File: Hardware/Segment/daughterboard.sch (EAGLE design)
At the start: 170 parts, among them IC1 PBQ79656PAPTQ1, IC2 PBQ79656PAPTQ1, T1 PBHV8115X, 115, T2 PBHV8115X, 115

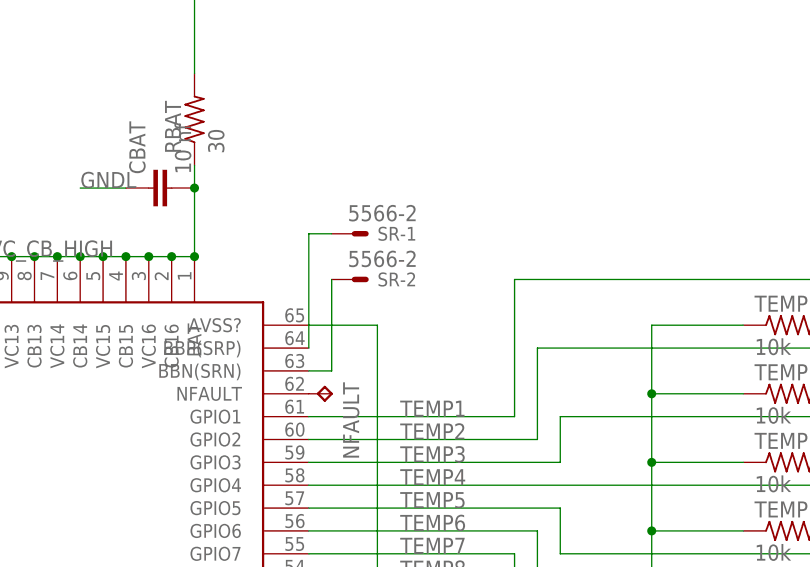
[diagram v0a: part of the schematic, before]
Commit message: Work on BQ library, RC fix for SR
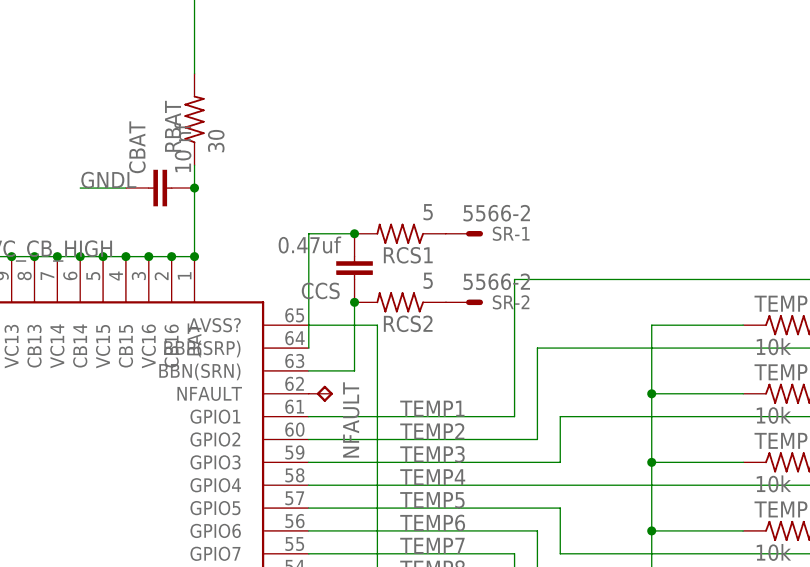
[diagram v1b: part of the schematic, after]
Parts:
- added CCS: 0.47uf, rcl:C-EUC0603
- added RCS1, RCS2: 5, rcl:R-US_R0603
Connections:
- new net N$13: RCS2.1, SR-2.S
- new net N$16: RCS1.1, SR-1.S
- net N$4: now also CCS.2, RCS1.2; no longer SR-1.S
- net N$7: now also CCS.1, RCS2.2; no longer SR-2.S
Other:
- moved on the sheet: SR-1, SR-2
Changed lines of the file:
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@@
 <part name="GND" library="wirepad" library_urn="urn:adsk.eagle:library:412" deviceset="2,54/1,0" device="" package3d_urn="urn:adsk.eagle:package:30828/1"/>
 <part name="NFAULT" library="testpad" library_urn="urn:adsk.eagle:library:385" deviceset="TP" device="B2,54" package3d_urn="urn:adsk.eagle:package:27948/1"/>
+<part name="RCS1" library="rcl" library_urn="urn:adsk.eagle:library:334" deviceset="R-US_" device="R0603" package3d_urn="urn:adsk.eagle:package:23555/3" value="5"/>
+<part name="RCS2" library="rcl" library_urn="urn:adsk.eagle:library:334" deviceset="R-US_" device="R0603" package3d_urn="urn:adsk.eagle:package:23555/3" value="5"/>
+<part name="CCS" library="rcl" library_urn="urn:adsk.eagle:library:334" deviceset="C-EU" device="C0603" package3d_urn="urn:adsk.eagle:package:23616/2" value="0.47uf"/>
 </parts>
 <sheets>
@@
 <attribute name="VALUE" x="181.737" y="198.882" size="1.778" layer="96" rot="R270"/>
 </instance>
-<instance part="SR" gate="-1" x="195.58" y="86.36" smashed="yes">
-<attribute name="NAME" x="198.12" y="85.598" size="1.524" layer="95"/>
-<attribute name="VALUE" x="194.818" y="87.757" size="1.778" layer="96"/>
-</instance>
-<instance part="SR" gate="-2" x="195.58" y="81.28" smashed="yes">
-<attribute name="NAME" x="198.12" y="80.518" size="1.524" layer="95"/>
-<attribute name="VALUE" x="194.818" y="82.677" size="1.778" layer="96"/>
+<instance part="SR" gate="-1" x="208.28" y="86.36" smashed="yes">
+<attribute name="NAME" x="210.82" y="85.598" size="1.524" layer="95"/>
+<attribute name="VALUE" x="207.518" y="87.757" size="1.778" layer="96"/>
+</instance>
+<instance part="SR" gate="-2" x="208.28" y="78.74" smashed="yes">
+<attribute name="NAME" x="210.82" y="77.978" size="1.524" layer="95"/>
+<attribute name="VALUE" x="207.518" y="80.137" size="1.778" layer="96"/>
 </instance>
 <instance part="DISABLE_UART" gate="1" x="175.26" y="43.18" smashed="yes">
@@
 <attribute name="TP_SIGNAL_NAME" x="191.77" y="67.31" size="1.778" layer="97" rot="R270"/>
 </instance>
+<instance part="RCS1" gate="G$1" x="200.66" y="86.36" smashed="yes" rot="R180">
+<attribute name="NAME" x="204.47" y="84.8614" size="1.778" layer="95" rot="R180"/>
+<attribute name="VALUE" x="204.47" y="89.662" size="1.778" layer="96" rot="R180"/>
+</instance>
+<instance part="RCS2" gate="G$1" x="200.66" y="78.74" smashed="yes" rot="R180">
+<attribute name="NAME" x="204.47" y="77.2414" size="1.778" layer="95" rot="R180"/>
+<attribute name="VALUE" x="204.47" y="82.042" size="1.778" layer="96" rot="R180"/>
+</instance>
+<instance part="CCS" gate="G$1" x="195.58" y="81.28" smashed="yes" rot="R180">
+<attribute name="NAME" x="194.056" y="80.899" size="1.778" layer="95" rot="R180"/>
+<attribute name="VALUE" x="194.056" y="85.979" size="1.778" layer="96" rot="R180"/>
+</instance>
 </instances>
 <busses>
@@
 <pinref part="IC1" gate="G$1" pin="BBP(SRP)"/>
 <wire x1="190.5" y1="73.66" x2="190.5" y2="86.36" width="0.1524" layer="91"/>
-<pinref part="SR" gate="-1" pin="S"/>
-<wire x1="190.5" y1="86.36" x2="193.04" y2="86.36" width="0.1524" layer="91"/>
+<pinref part="CCS" gate="G$1" pin="2"/>
+<pinref part="RCS1" gate="G$1" pin="2"/>
+<wire x1="190.5" y1="86.36" x2="195.58" y2="86.36" width="0.1524" layer="91"/>
+<junction x="195.58" y="86.36"/>
 </segment>
 </net>
 <net name="N$7" class="0">
 <segment>
-<pinref part="SR" gate="-2" pin="S"/>
-<wire x1="193.04" y1="81.28" x2="193.04" y2="71.12" width="0.1524" layer="91"/>
 <pinref part="IC1" gate="G$1" pin="BBN(SRN)"/>
-<wire x1="193.04" y1="71.12" x2="190.5" y2="71.12" width="0.1524" layer="91"/>
+<pinref part="CCS" gate="G$1" pin="1"/>
+<pinref part="RCS2" gate="G$1" pin="2"/>
+<wire x1="190.5" y1="71.12" x2="195.58" y2="71.12" width="0.1524" layer="91"/>
+<wire x1="195.58" y1="71.12" x2="195.58" y2="78.74" width="0.1524" layer="91"/>
+<junction x="195.58" y="78.74"/>
 </segment>
 </net>
@@
 </segment>
 </net>
+<net name="N$13" class="0">
+<segment>
+<pinref part="RCS2" gate="G$1" pin="1"/>
+<pinref part="SR" gate="-2" pin="S"/>
+</segment>
+</net>
+<net name="N$16" class="0">
+<segment>
+<pinref part="SR" gate="-1" pin="S"/>
+<pinref part="RCS1" gate="G$1" pin="1"/>
+</segment>
+</net>

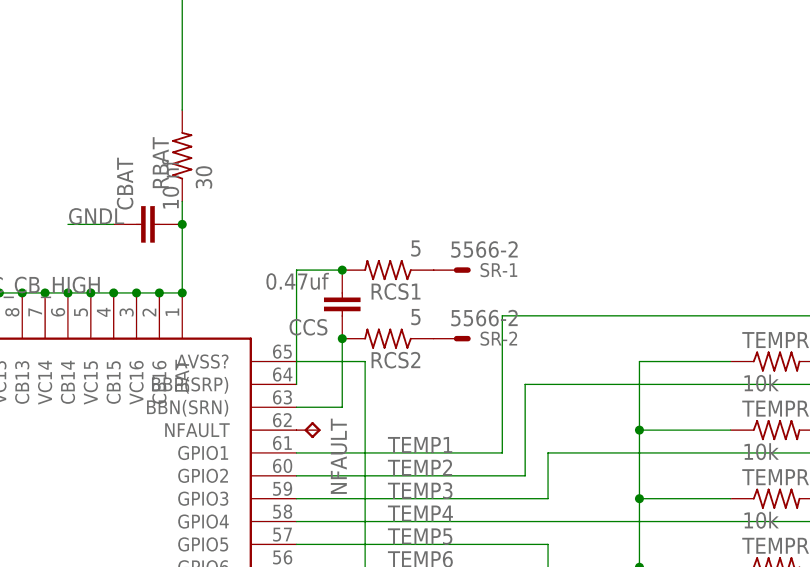
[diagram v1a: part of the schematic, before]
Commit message: ESP32-devkitc-32D instead ov DEVKIT V1
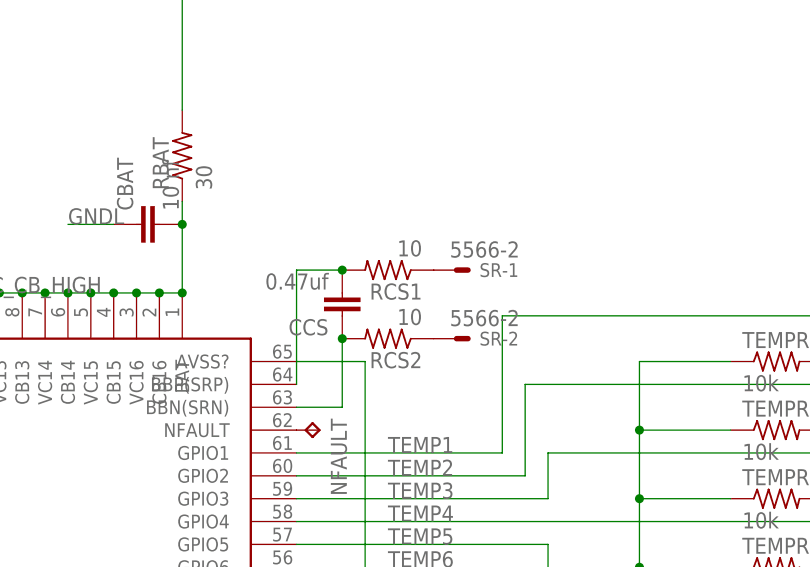
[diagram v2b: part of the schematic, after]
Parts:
- RCS1, RCS2: value 5 -> 10
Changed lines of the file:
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@@
 <part name="GND" library="wirepad" library_urn="urn:adsk.eagle:library:412" deviceset="2,54/1,0" device="" package3d_urn="urn:adsk.eagle:package:30828/1"/>
 <part name="NFAULT" library="testpad" library_urn="urn:adsk.eagle:library:385" deviceset="TP" device="B2,54" package3d_urn="urn:adsk.eagle:package:27948/1"/>
-<part name="RCS1" library="rcl" library_urn="urn:adsk.eagle:library:334" deviceset="R-US_" device="R0603" package3d_urn="urn:adsk.eagle:package:23555/3" value="5"/>
-<part name="RCS2" library="rcl" library_urn="urn:adsk.eagle:library:334" deviceset="R-US_" device="R0603" package3d_urn="urn:adsk.eagle:package:23555/3" value="5"/>
+<part name="RCS1" library="rcl" library_urn="urn:adsk.eagle:library:334" deviceset="R-US_" device="R0603" package3d_urn="urn:adsk.eagle:package:23555/3" value="10"/>
+<part name="RCS2" library="rcl" library_urn="urn:adsk.eagle:library:334" deviceset="R-US_" device="R0603" package3d_urn="urn:adsk.eagle:package:23555/3" value="10"/>
 <part name="CCS" library="rcl" library_urn="urn:adsk.eagle:library:334" deviceset="C-EU" device="C0603" package3d_urn="urn:adsk.eagle:package:23616/2" value="0.47uf"/>
 </parts>

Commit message: Fixed resistors in layout, moved connectors from edge
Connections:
- removed net N$100: CVC0-1.1, CVC1-1.2, RVC1-1.1, VCH-2.S
- removed net N$101: CVC1-1.1, CVC2-1.2, RVC2-1.1, VCH-3.S
- removed net N$102: CVC2-1.1, CVC3-1.2, RVC3-1.1, VCH-4.S
- removed net N$103: CVC3-1.1, CVC4-1.2, RVC4-1.1, VCH-5.S
- removed net N$104: CVC4-1.1, CVC5-1.2, RVC5-1.1, VCH-6.S
- removed net N$105: CVC5-1.1, CVC6-1.2, RVC6-1.1, VCH-7.S
- removed net N$106: CVC6-1.1, CVC7-1.2, RVC7-1.1, VCH-8.S
- removed net N$107: CVC7-1.1, CVC8-1.2, RVC8-1.1, VCH-9.S
- removed net N$108: CVC8-1.1, CVC9-1.2, RVC9-1.1, VCH-10.S
- removed net N$109: CVC9-1.1, RVC10-1.1, VCH-11.S
- removed net N$43: CVC8.1, CVC9.2, RVC9.1, VCL-10.S
- removed net N$44: CVC9.1, RVC10.1, VCL-11.S
- removed net N$99: CVC0-1.2, RVC0-1.1, VCH-1.S
- new net N$11: CBL-11.S, RCB10.1
- new net N$17: CBH-11.S, RCB10-1.1
- new net N$19: RVC1.1, VCL-2.S
- new net N$20: RVC2.1, VCL-3.S
- new net N$22: RVC3.1, VCL-4.S
- new net N$23: RVC4.1, VCL-5.S
- new net N$24: RVC9.1, VCL-10.S
- new net N$25: RVC8.1, VCL-9.S
- new net N$26: RVC7.1, VCL-8.S
- new net N$28: RVC6.1, VCL-7.S
- new net N$30: RVC5.1, VCL-6.S
- new net N$32: CBL-1.S, RCB0.1
- new net N$96: CBH-1.S, RCB0-1.1
- net BATC: now also RVC10.1, VCL-11.S; no longer CBL-11.S, RCB10.1
- net BATC-1: now also RVC10-1.1, VCH-11.S; no longer CBH-11.S, RCB10-1.1
- net GNDH: now also RVC0-1.1, VCH-1.S; no longer CBH-1.S, RCB0-1.1
- net GNDL: now also RVC0.1, VCL-1.S; no longer CBL-1.S, RCB0.1
- net N$34: now also RVC9-1.1, VCH-10.S; no longer CVC0.2, RVC0.1, VCL-1.S
- net N$35: now also RVC8-1.1, VCH-9.S; no longer CVC0.1, CVC1.2, RVC1.1, VCL-2.S
- net N$36: now also RVC7-1.1, VCH-8.S; no longer CVC1.1, CVC2.2, RVC2.1, VCL-3.S
- net N$37: now also RVC6-1.1, VCH-7.S; no longer CVC2.1, CVC3.2, RVC3.1, VCL-4.S
- net N$38: now also RVC5-1.1, VCH-6.S; no longer CVC3.1, CVC4.2, RVC4.1, VCL-5.S
- net N$39: now also RVC4-1.1, VCH-5.S; no longer CVC4.1, CVC5.2, RVC5.1, VCL-6.S
- net N$40: now also RVC3-1.1, VCH-4.S; no longer CVC5.1, CVC6.2, RVC6.1, VCL-7.S
- net N$41: now also RVC2-1.1, VCH-3.S; no longer CVC6.1, CVC7.2, RVC7.1, VCL-8.S
- net N$42: now also RVC1-1.1, VCH-2.S; no longer CVC7.1, CVC8.2, RVC8.1, VCL-9.S
- net VC0: now also CVC0.2
- net VC0-1: now also CVC0-1.2
- net VC1: now also CVC0.1, CVC1.2
- net VC1-1: now also CVC0-1.1, CVC1-1.2
- net VC10: now also CVC9.1
- net VC10-1: now also CVC9-1.1
- net VC2: now also CVC1.1, CVC2.2
- net VC2-1: now also CVC1-1.1, CVC2-1.2
- net VC3: now also CVC2.1, CVC3.2
- net VC3-1: now also CVC2-1.1, CVC3-1.2
- net VC4: now also CVC3.1, CVC4.2
- net VC4-1: now also CVC3-1.1, CVC4-1.2
- net VC5: now also CVC4.1, CVC5.2
- net VC5-1: now also CVC4-1.1, CVC5-1.2
- net VC6: now also CVC5.1, CVC6.2
- net VC6-1: now also CVC5-1.1, CVC6-1.2
- net VC7: now also CVC6.1, CVC7.2
- net VC7-1: now also CVC6-1.1, CVC7-1.2
- net VC8: now also CVC7.1, CVC8.2
- net VC8-1: now also CVC7-1.1, CVC8-1.2
- net VC9: now also CVC8.1, CVC9.2
- net VC9-1: now also CVC8-1.1, CVC9-1.2
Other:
- moved on the sheet: CVC0, CVC0-1, CVC1, CVC1-1, CVC2, CVC2-1, CVC3, CVC3-1, CVC4, CVC4-1, CVC5, CVC5-1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

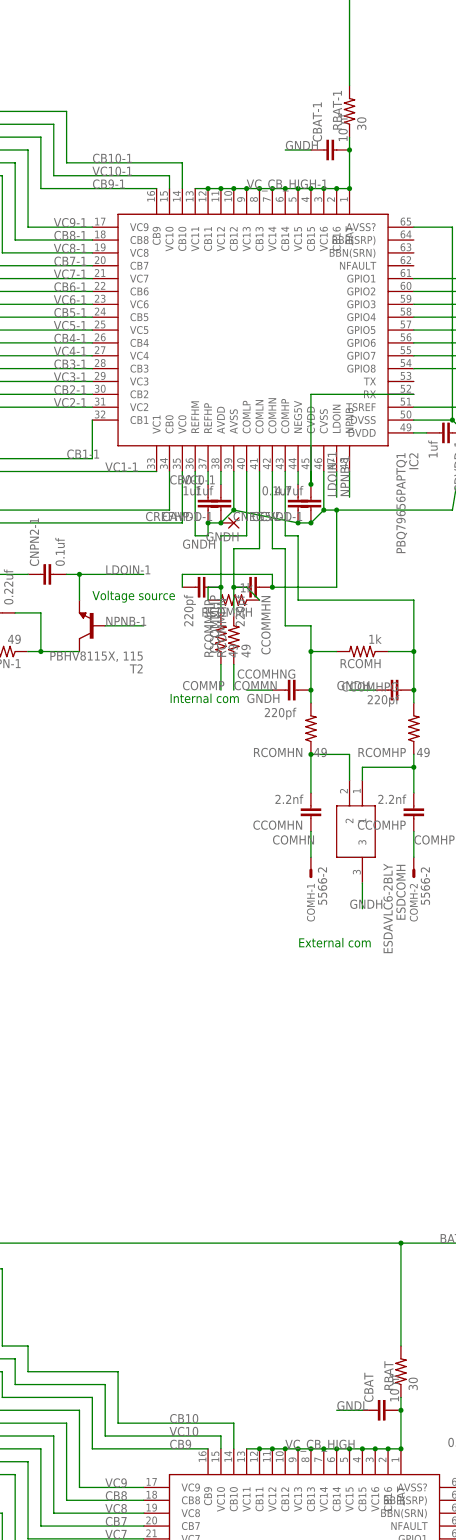
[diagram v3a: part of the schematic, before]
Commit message: Schematic progress for mainboard
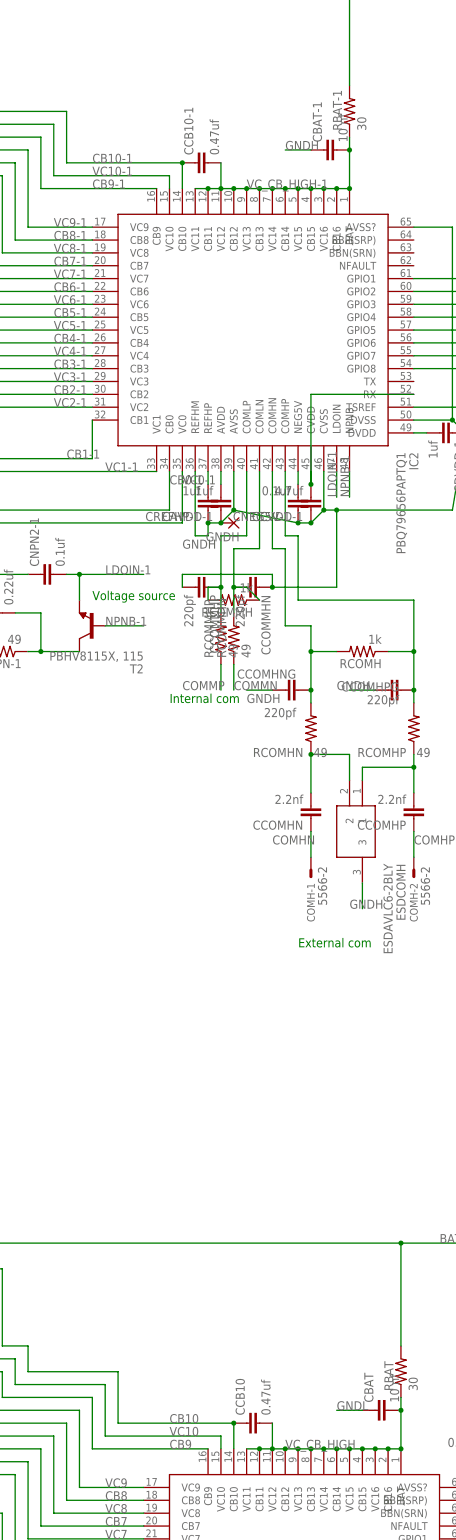
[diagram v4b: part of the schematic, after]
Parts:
- added CCB10, CCB10-1: 0.47uf, rcl:C-EUC0603
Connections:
- net CB10: now also CCB10.1
- net CB10-1: now also CCB10-1.1
- net VC_CB_HIGH: now also CCB10.2
- net VC_CB_HIGH-1: now also CCB10-1.2
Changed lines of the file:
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@@
 <part name="RCS2" library="rcl" library_urn="urn:adsk.eagle:library:334" deviceset="R-US_" device="R0603" package3d_urn="urn:adsk.eagle:package:23555/3" value="10"/>
 <part name="CCS" library="rcl" library_urn="urn:adsk.eagle:library:334" deviceset="C-EU" device="C0603" package3d_urn="urn:adsk.eagle:package:23616/2" value="0.47uf"/>
+<part name="CCB10" library="rcl" library_urn="urn:adsk.eagle:library:334" deviceset="C-EU" device="C0603" package3d_urn="urn:adsk.eagle:package:23616/2" value="0.47uf"/>
+<part name="CCB10-1" library="rcl" library_urn="urn:adsk.eagle:library:334" deviceset="C-EU" device="C0603" package3d_urn="urn:adsk.eagle:package:23616/2" value="0.47uf"/>
 </parts>
 <sheets>
@@
 <attribute name="VALUE" x="194.056" y="85.979" size="1.778" layer="96" rot="R180"/>
 </instance>
+<instance part="CCB10" gate="G$1" x="147.32" y="88.9" smashed="yes" rot="R90">
+<attribute name="NAME" x="146.939" y="90.424" size="1.778" layer="95" rot="R90"/>
+<attribute name="VALUE" x="152.019" y="90.424" size="1.778" layer="96" rot="R90"/>
+</instance>
+<instance part="CCB10-1" gate="G$1" x="137.16" y="337.82" smashed="yes" rot="R90">
+<attribute name="NAME" x="136.779" y="339.344" size="1.778" layer="95" rot="R90"/>
+<attribute name="VALUE" x="141.859" y="339.344" size="1.778" layer="96" rot="R90"/>
+</instance>
 </instances>
 <busses>
@@
 <junction x="83.82" y="119.38"/>
 <label x="132.08" y="88.9" size="1.778" layer="95"/>
+<pinref part="CCB10" gate="G$1" pin="1"/>
+<junction x="144.78" y="88.9"/>
 </segment>
 </net>
@@
 <junction x="177.8" y="91.44"/>
 <label x="154.94" y="83.82" size="1.778" layer="95"/>
+<pinref part="CCB10" gate="G$1" pin="2"/>
+<wire x1="152.4" y1="88.9" x2="152.4" y2="83.82" width="0.1524" layer="91"/>
 </segment>
 </net>
@@
 <junction x="73.66" y="368.3"/>
 <label x="116.84" y="337.82" size="1.778" layer="95"/>
+<pinref part="CCB10-1" gate="G$1" pin="1"/>
+<junction x="134.62" y="337.82"/>
 </segment>
 </net>
@@
 <junction x="167.64" y="340.36"/>
 <label x="147.32" y="332.74" size="1.778" layer="95"/>
-</segment>
-</net>
+<pinref part="CCB10-1" gate="G$1" pin="2"/>
+<wire x1="142.24" y1="337.82" x2="142.24" y2="332.74" width="0.1524" layer="91"/>
+</segment>
+</net>
